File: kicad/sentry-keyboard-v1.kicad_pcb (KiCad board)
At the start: 2 copper layers, 315 x 121 mm, 269 parts, among them J2 Conn_01x04, J4 AVR-ISP-6, SW1 Reset, SW2 RotaryEncoder_Switch, U1 ATmega32U4-AU, Y1 16Mhz

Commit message: More LED routing
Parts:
- moved C5 4.58 mm to (219.5, 199.5)
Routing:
- net +5V: track 149.7 -> 1694.0 mm, vias 0 -> 4
- net Net-(J4-~{RST}): track 0.00 -> 73.8 mm, vias 0 -> 2
- net Row4: track 349.6 -> 387.6 mm, vias 2 -> 4
- net Row2: track 271.4 -> 283.8 mm
- net Row5: track 269.3 -> 281.1 mm
- net Col4: track 181.5 -> 191.2 mm
- net Net-(D76-A): track 0.62 -> 7.43 mm
- net Net-(U1-XTAL2): track 0.00 -> 3.80 mm

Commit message: More routing
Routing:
- net +5V: track 1694.0 -> 1769.1 mm, vias 4 -> 2
- net GND: track 3.10 -> 49.5 mm
- net Net-(U1-UCAP): track 0.00 -> 11.9 mm
- net Row2: track 283.8 -> 272.2 mm
- net Net-(U1-XTAL1): track 0.00 -> 4.08 mm
- net Net-(D89-DOUT): track 66.8 -> 67.8 mm
- net Net-(D88-DOUT): vias 0 -> 2

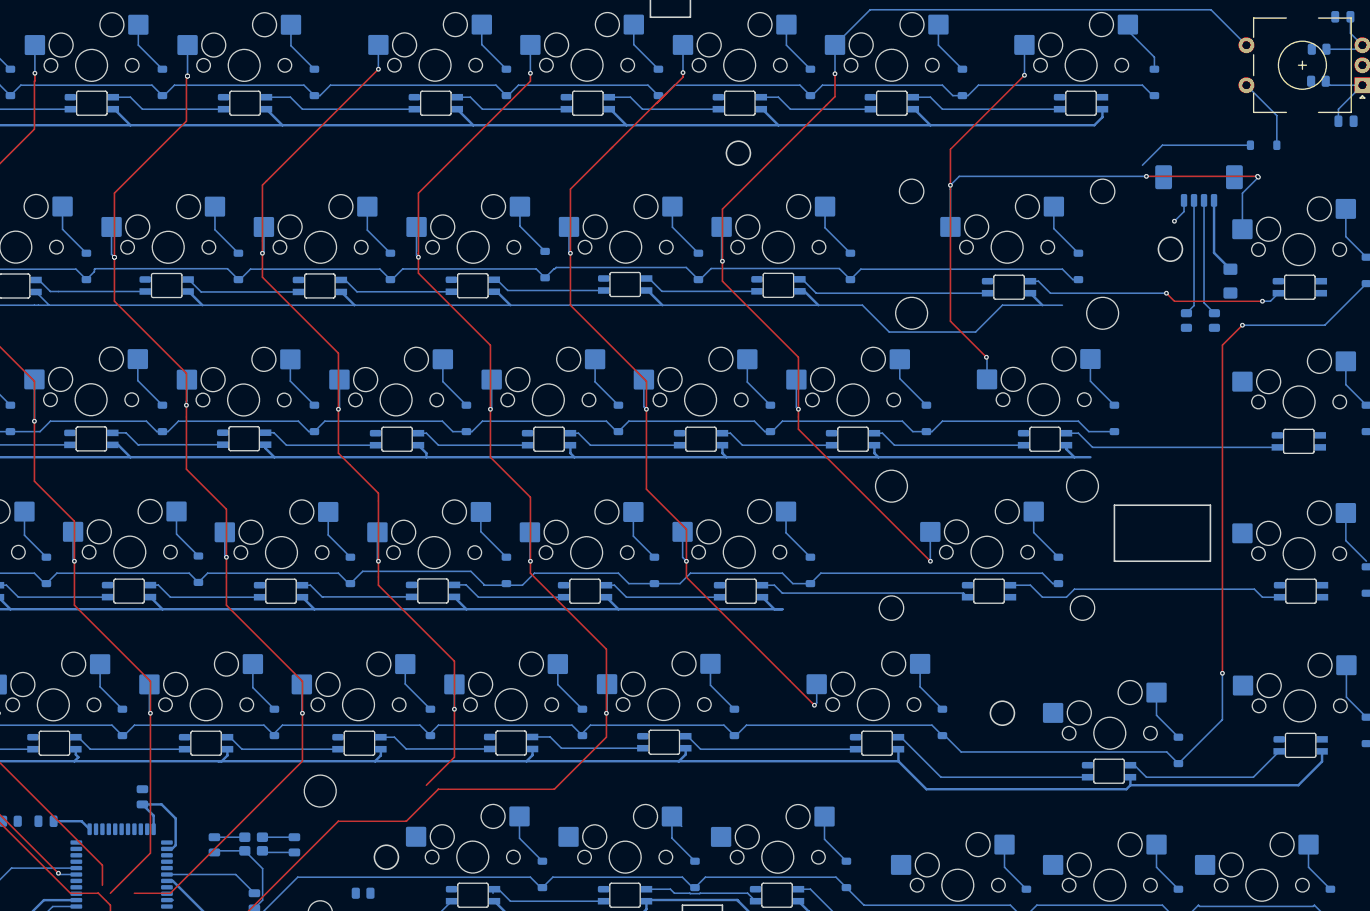
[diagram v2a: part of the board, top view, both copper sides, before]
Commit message: Route 5v from connector to cpu
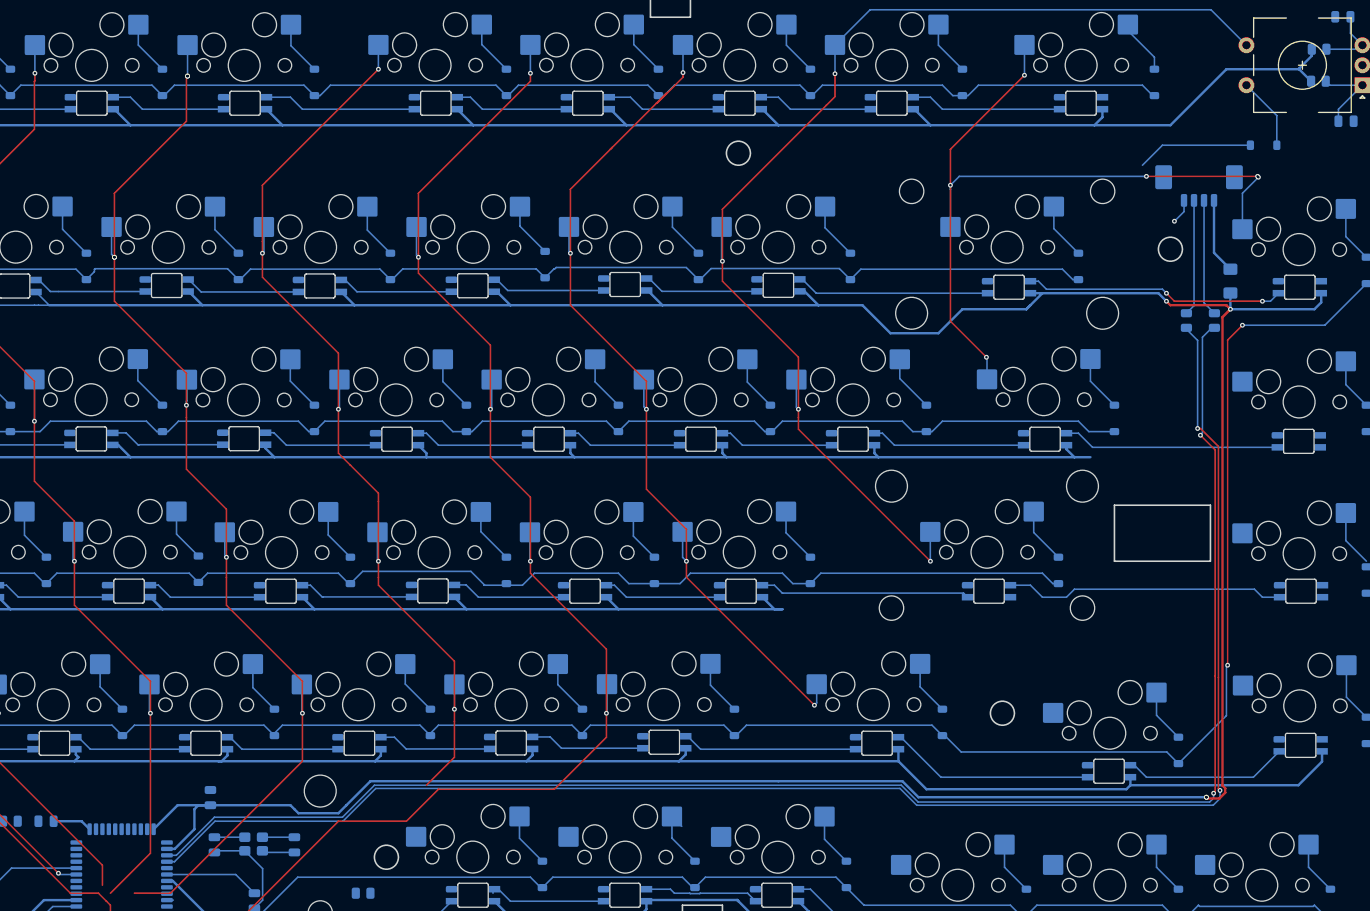
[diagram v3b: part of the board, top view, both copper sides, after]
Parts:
- moved C4 8.50 mm to (219.5, 182.1)
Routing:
- net +5V: track 1769.1 -> 2035.8 mm, vias 2 -> 6
- net D+: track 0.00 -> 197.4 mm, vias 0 -> 2
- net D-: track 0.00 -> 196.1 mm, vias 0 -> 2

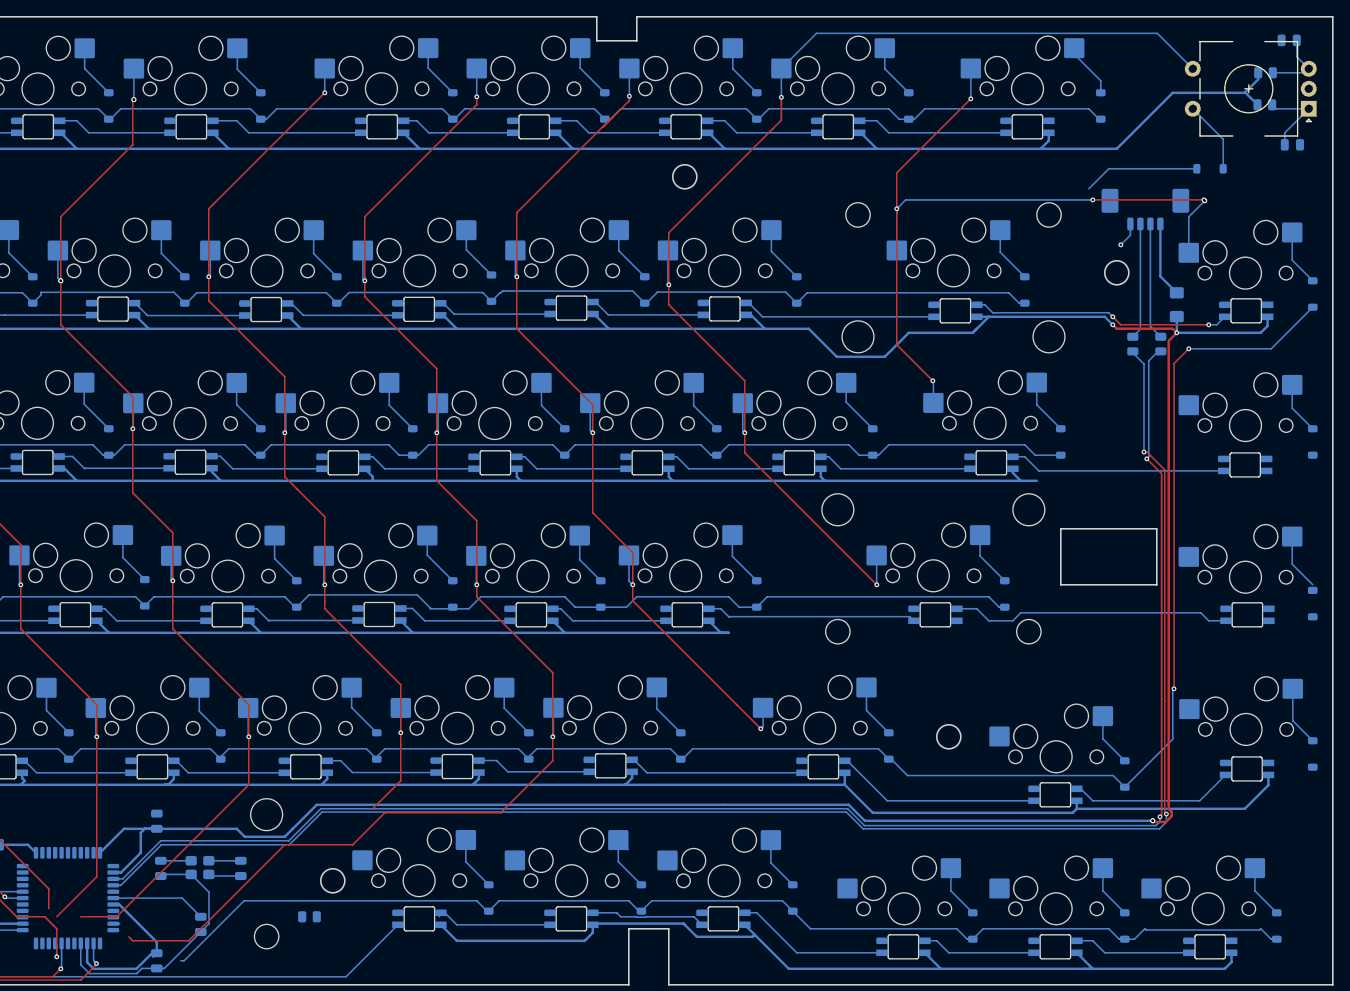
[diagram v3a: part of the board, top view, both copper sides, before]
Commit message: More routing progress
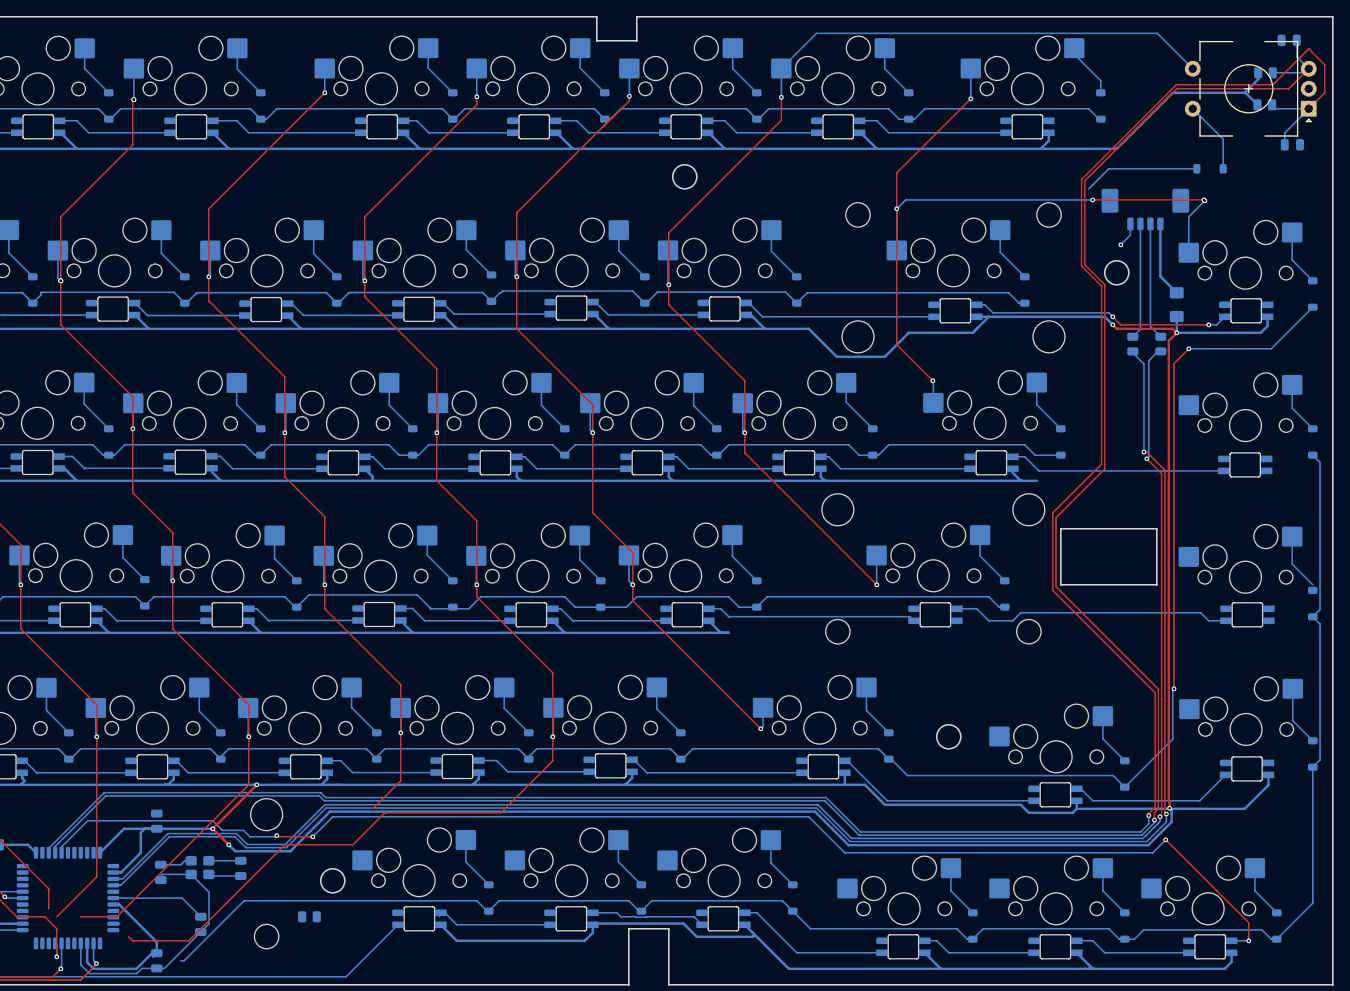
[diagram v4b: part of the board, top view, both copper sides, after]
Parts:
- moved C2 0.50 mm to (220.0, 188.4)
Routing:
- net Encoder A: track 10.5 -> 288.0 mm, vias 0 -> 1
- net Encoder B: track 8.88 -> 275.5 mm, vias 0 -> 1
- net LED-DIN: track 0.00 -> 163.7 mm, vias 0 -> 4
- net Row5: track 281.3 -> 344.9 mm
- net +5V: track 2035.8 -> 2047.3 mm, vias 6 -> 8
- net D-: track 196.1 -> 198.9 mm
- net D+: track 197.4 -> 200.3 mm

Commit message: Route more of 5V lines
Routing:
- net +5V: track 2047.3 -> 2248.1 mm, vias 8 -> 12
- net Net-(U1-~{HWB}/PE2): track 0.00 -> 8.43 mm
- net Col13: vias 6 -> 5

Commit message: Add led switch backs.
hopefully the distance doesn't matter too much
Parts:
- moved R6 0.50 mm to (344.5, 122.4)
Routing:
- net Net-(D135-DOUT): track 0.00 -> 335.8 mm, vias 0 -> 2
- net Net-(D92-DOUT): track 0.00 -> 333.4 mm
- net Net-(D106-DOUT): track 0.00 -> 333.2 mm
- net Net-(D120-DOUT): track 0.00 -> 323.7 mm
- net Net-(D150-DOUT): track 0.00 -> 305.9 mm, vias 0 -> 2
- net +5V: track 2248.1 -> 2258.2 mm, vias 12 -> 13
- net Col0: track 123.6 -> 121.6 mm
- net D-: track 198.9 -> 199.6 mm

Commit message: More routing progress
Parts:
- moved R1 65.2 mm to (173.5, 197.0), turned to 90 degrees
- moved C3 8.54 mm to (222.0, 186.9), turned to 90 degrees
- moved C7 6.44 mm to (199.0, 194.4)
- moved C1 5.22 mm to (231.5, 192.9)
- moved Y1 5.22 mm to (226.4, 192.8)
- moved C2 4.37 mm to (221.5, 192.6)
- moved C5 2.07 mm to (220.1, 197.5), turned to 0 degrees
- moved U1 2.05 mm to (209.8, 190.2)
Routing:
- net Col0: track 121.6 -> 307.5 mm, vias 6 -> 7
- net Col1: track 135.7 -> 284.0 mm, vias 6 -> 7
- net Col5: track 164.6 -> 277.2 mm, vias 6 -> 8
- net Col7: track 138.5 -> 223.1 mm
- net Col6: track 140.2 -> 203.8 mm
- net Row5: track 344.9 -> 392.2 mm
- net Col3: track 159.9 -> 194.9 mm
- net Net-(J4-~{RST}): track 74.1 -> 45.0 mm
- net Net-(U1-XTAL1): track 4.08 -> 28.7 mm
- net Net-(U1-XTAL2): track 4.01 -> 28.0 mm
- net Col10: track 179.6 -> 198.1 mm, vias 5 -> 6
- net LED-DIN: track 163.7 -> 158.5 mm
- net Net-(U1-UCAP): track 11.9 -> 7.47 mm
- net Col4: track 191.2 -> 187.2 mm, vias 6 -> 5
- net Col8: track 144.9 -> 148.7 mm
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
